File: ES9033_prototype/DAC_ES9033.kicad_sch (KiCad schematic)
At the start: 29 parts, among them U201 ES9033, X201 ECS-2520MV-xxx-xx

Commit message: added schematic title
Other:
- company: (none) -> Fabian Muehlberger 
- title: (none) -> ES9033 DAC prototype
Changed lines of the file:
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@@
 (kicad_sch (version 20211123) (generator eeschema)
   (paper "A4")
+  (title_block
+    (title "ES9033 DAC prototype")
+    (date "2022-09-09")
+    (rev "0.1")
+    (company "Fabian Muehlberger ")
+  )
   (junction (at 140.97 78.74) (diameter 0) (color 0 0 0 0)
   )

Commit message: changed header
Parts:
- added J3: Conn_02x02_Counter_Clockwise, Connector_PinHeader_2.54mm:PinHeader_2x02_P2.54mm_Vertical, symbol Connector_Generic:Conn_02x02_Counter_Clockwise
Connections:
- net DAC_MCLK: no longer names the net of X201.3 (OUT)
- net DAC_MCLK: now also J3.1 (Pin_1), J3.2 (Pin_2); no longer U201.26 (MCLK/GPIO)
- new net MCLK: J3.3 (Pin_3)
- new net MCLK_DAC_IN: J3.4 (Pin_4), U201.26 (MCLK/GPIO)
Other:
- moved on the sheet: C201, C202, C203, C204, C205, C206, C207, C208, C209, C210, C211, NT201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

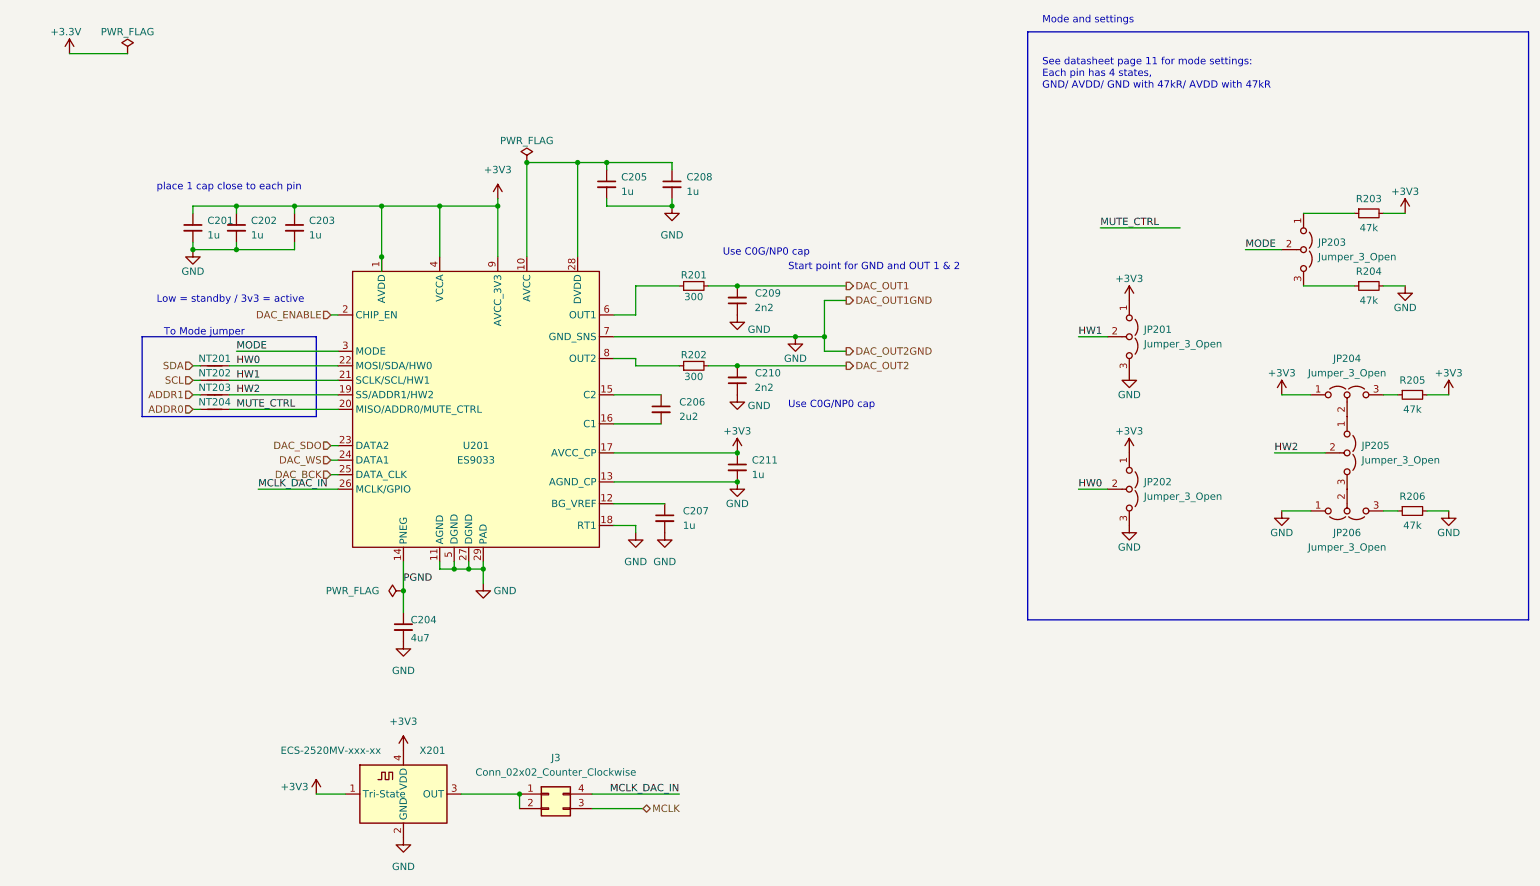
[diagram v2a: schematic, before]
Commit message: changed header placement
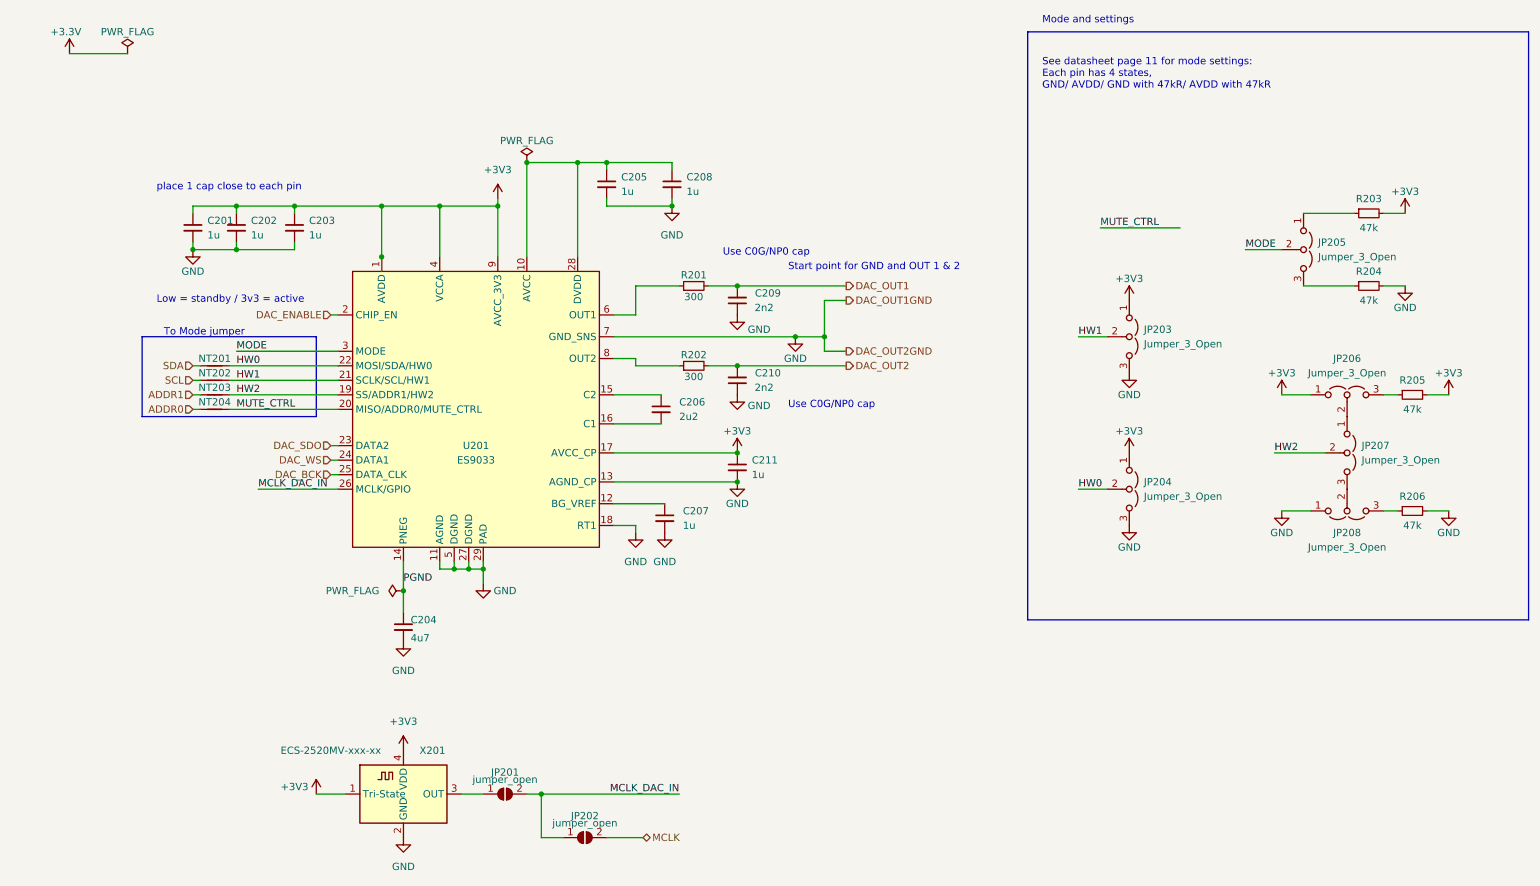
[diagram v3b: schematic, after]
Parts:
- removed J3: Conn_02x02_Counter_Clockwise, Connector_PinHeader_2.54mm:PinHeader_2x02_P2.54mm_Vertical, symbol Connector_Generic:Conn_02x02_Counter_Clockwise
- added JP201, JP202: jumper_open, Jumper:SolderJumper-2_P1.3mm_Open_Pad1.0x1.5mm, symbol Jumper:SolderJumper_2_Open
- renumbered JP201 to JP203, JP202 to JP204, JP203 to JP205, JP204 to JP206, JP205 to JP207, JP206 to JP208
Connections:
- net MCLK: now also JP202.2 (B)
- net MCLK_DAC_IN: now also JP201.2 (B), JP202.1 (A)
- net at X201.3 (OUT): now also JP201.1 (A)

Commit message: stuff
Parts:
- added SW201: SW_SP3T, Button_Switch_SMD:SW_SP3T_PCM13, symbol Switch:SW_SP3T
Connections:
- net +3V3: now also SW201.4
- net DAC_ENABLE: now also SW201.2; no longer U201.2 (CHIP_EN)
- net GND: now also SW201.1
- new net: SW201.3, U201.2 (CHIP_EN)
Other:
- moved on the sheet: C201, C202, C203, NT201, NT202, NT203, NT204
